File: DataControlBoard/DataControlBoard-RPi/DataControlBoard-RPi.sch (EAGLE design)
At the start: 6 parts, among them J1 USB3150-30-130-A, J2 USB3150-30-130-A, J3 USB3150-30-130-A, J4 USB3150-30-130-A, J5 USB3150-30-130-A, J6 USB3150-30-130-A

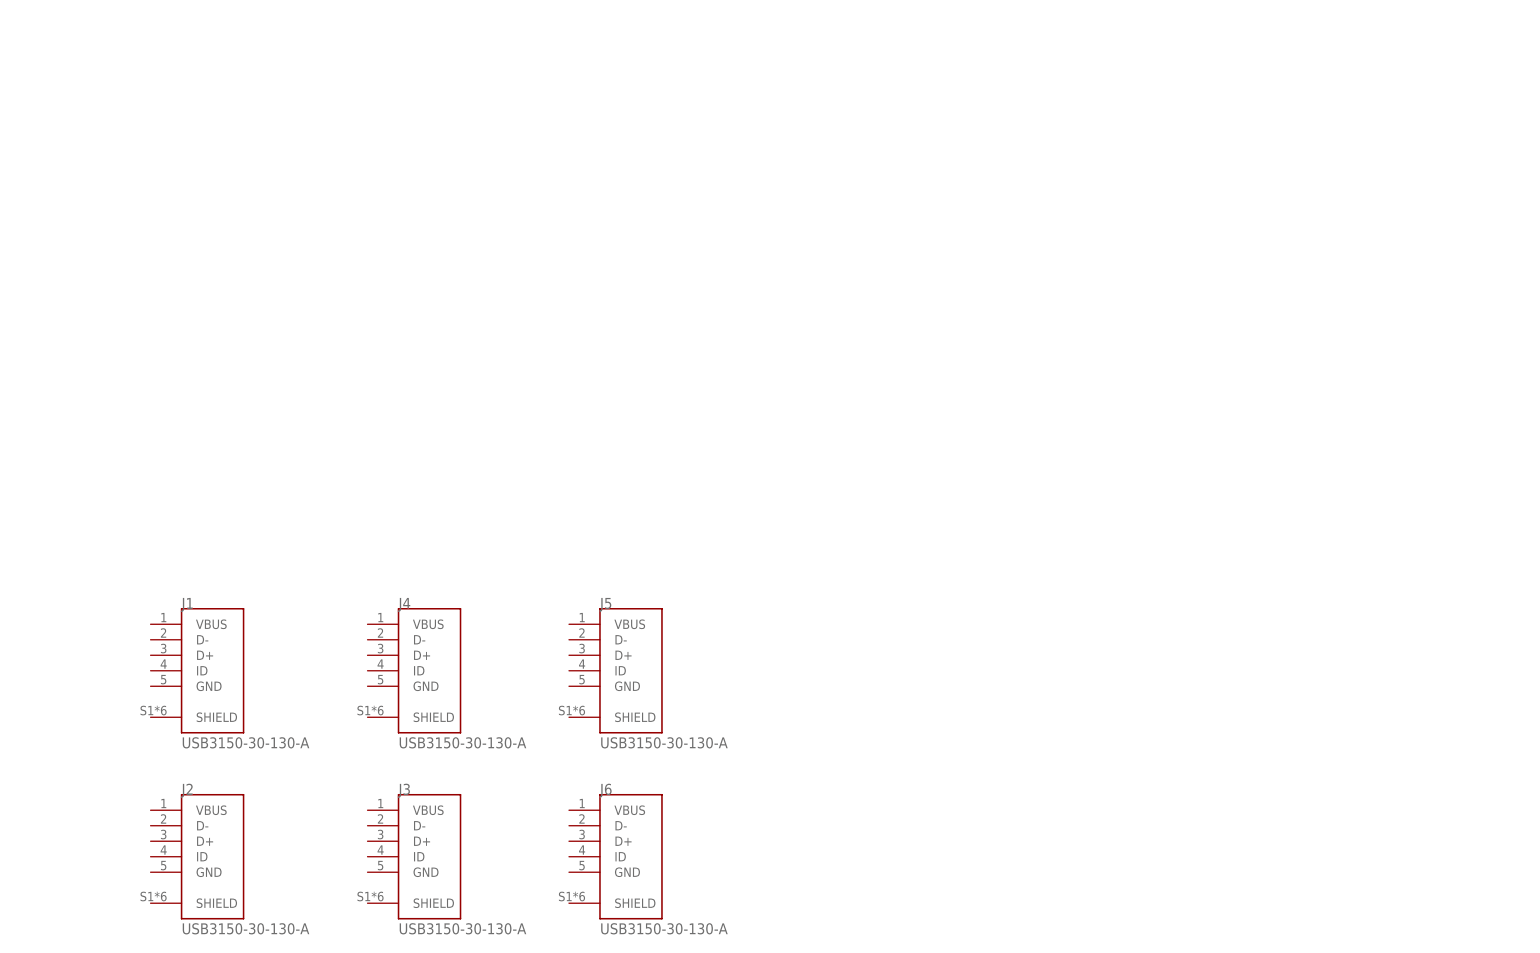
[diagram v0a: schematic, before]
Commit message: Added data control boards, further refined USB part
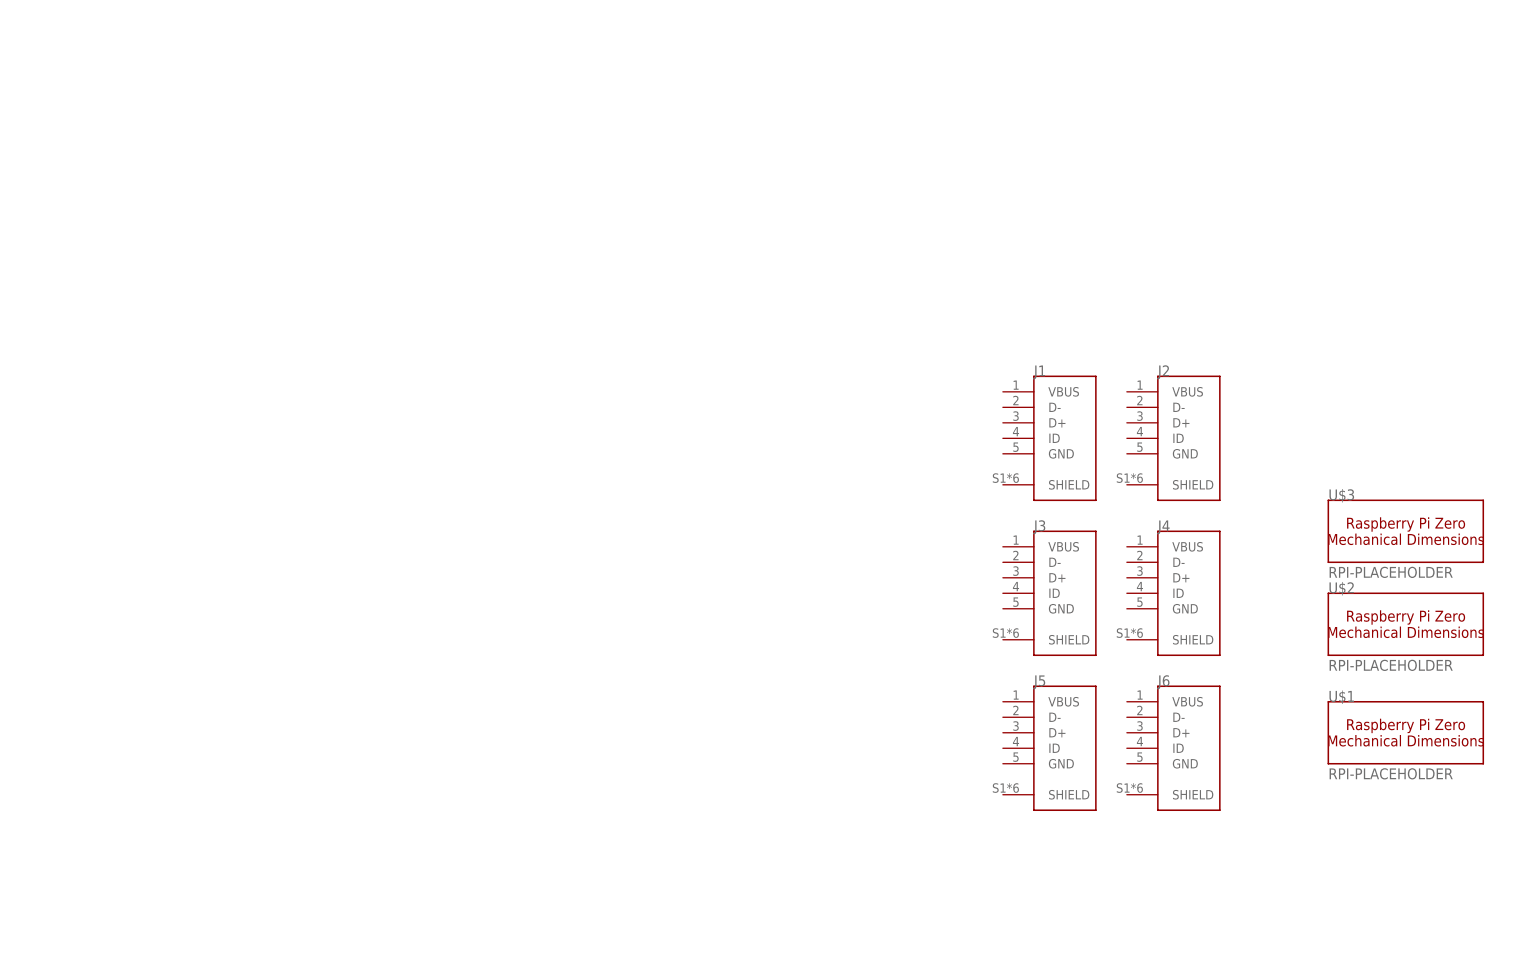
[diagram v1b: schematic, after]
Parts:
- added U$1, U$2, U$3: RPI-PLACEHOLDER, RPi-Parts:RPI-PLACEHOLDER
- J1, J2, J3, J4, J5, J6: value USB3150-30-130-A -> USB3150-30-130-AMANUFACTURABLE; device USB3150-30-130-A:USB3150-30-130-A -> RPi-Parts:USB3150-30-130-AMANUFACTURABLE
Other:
- moved on the sheet: J1, J2, J3, J4, J5, J6
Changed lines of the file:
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@@
 <layer number="97" name="Info" color="7" fill="1" visible="yes" active="yes"/>
 <layer number="98" name="Guide" color="6" fill="1" visible="yes" active="yes"/>
+<layer number="200" name="RPI-DIMS" color="39" fill="7" visible="yes" active="yes"/>
+<layer number="201" name="RPI-PORTS" color="22" fill="5" visible="yes" active="yes"/>
+<layer number="202" name="RPI-Mounting" color="23" fill="10" visible="yes" active="yes"/>
 </layers>
 <schematic xreflabel="%F%N/%S.%C%R" xrefpart="/%S.%C%R">
@@
 </classes>
 <parts>
-<part name="J1" library="USB3150-30-130-A" deviceset="USB3150-30-130-A" device=""/>
-<part name="J2" library="USB3150-30-130-A" deviceset="USB3150-30-130-A" device=""/>
-<part name="J3" library="USB3150-30-130-A" deviceset="USB3150-30-130-A" device=""/>
-<part name="J4" library="USB3150-30-130-A" deviceset="USB3150-30-130-A" device=""/>
-<part name="J5" library="USB3150-30-130-A" deviceset="USB3150-30-130-A" device=""/>
-<part name="J6" library="USB3150-30-130-A" deviceset="USB3150-30-130-A" device=""/>
 <part name="FRAME1" library="frames" library_urn="urn:adsk.eagle:library:229" deviceset="A4L-LOC" device=""/>
+<part name="U$1" library="RPi-Parts" deviceset="RPI-PLACEHOLDER" device=""/>
+<part name="U$2" library="RPi-Parts" deviceset="RPI-PLACEHOLDER" device=""/>
+<part name="U$3" library="RPi-Parts" deviceset="RPI-PLACEHOLDER" device=""/>
+<part name="J1" library="RPi-Parts" deviceset="USB3150-30-130-A" device="MANUFACTURABLE"/>
+<part name="J2" library="RPi-Parts" deviceset="USB3150-30-130-A" device="MANUFACTURABLE"/>
+<part name="J3" library="RPi-Parts" deviceset="USB3150-30-130-A" device="MANUFACTURABLE"/>
+<part name="J4" library="RPi-Parts" deviceset="USB3150-30-130-A" device="MANUFACTURABLE"/>
+<part name="J5" library="RPi-Parts" deviceset="USB3150-30-130-A" device="MANUFACTURABLE"/>
+<part name="J6" library="RPi-Parts" deviceset="USB3150-30-130-A" device="MANUFACTURABLE"/>
 </parts>
 <sheets>
@@
 </plain>
 <instances>
-<instance part="J1" gate="G$1" x="40.64" y="63.5" smashed="yes">
-<attribute name="NAME" x="35.56" y="73.66" size="1.778" layer="95"/>
-<attribute name="VALUE" x="35.56" y="50.8" size="1.778" layer="96"/>
-</instance>
-<instance part="J2" gate="G$1" x="40.64" y="33.02" smashed="yes">
-<attribute name="NAME" x="35.56" y="43.18" size="1.778" layer="95"/>
-<attribute name="VALUE" x="35.56" y="20.32" size="1.778" layer="96"/>
-</instance>
-<instance part="J3" gate="G$1" x="76.2" y="33.02" smashed="yes">
-<attribute name="NAME" x="71.12" y="43.18" size="1.778" layer="95"/>
-<attribute name="VALUE" x="71.12" y="20.32" size="1.778" layer="96"/>
-</instance>
-<instance part="J4" gate="G$1" x="76.2" y="63.5" smashed="yes">
-<attribute name="NAME" x="71.12" y="73.66" size="1.778" layer="95"/>
-<attribute name="VALUE" x="71.12" y="50.8" size="1.778" layer="96"/>
-</instance>
-<instance part="J5" gate="G$1" x="109.22" y="63.5" smashed="yes">
-<attribute name="NAME" x="104.14" y="73.66" size="1.778" layer="95"/>
-<attribute name="VALUE" x="104.14" y="50.8" size="1.778" layer="96"/>
-</instance>
-<instance part="J6" gate="G$1" x="109.22" y="33.02" smashed="yes">
-<attribute name="NAME" x="104.14" y="43.18" size="1.778" layer="95"/>
-<attribute name="VALUE" x="104.14" y="20.32" size="1.778" layer="96"/>
-</instance>
 <instance part="FRAME1" gate="G$1" x="0" y="0" smashed="yes">
 <attribute name="DRAWING_NAME" x="217.17" y="15.24" size="2.54" layer="94"/>
 <attribute name="LAST_DATE_TIME" x="217.17" y="10.16" size="2.286" layer="94"/>
 <attribute name="SHEET" x="230.505" y="5.08" size="2.54" layer="94"/>
+</instance>
+<instance part="U$1" gate="G$1" x="236.22" y="53.34" smashed="yes">
+<attribute name="NAME" x="223.52" y="58.42" size="1.778" layer="95"/>
+<attribute name="VALUE" x="223.52" y="45.72" size="1.778" layer="95"/>
+</instance>
+<instance part="U$2" gate="G$1" x="236.22" y="71.12" smashed="yes">
+<attribute name="NAME" x="223.52" y="76.2" size="1.778" layer="95"/>
+<attribute name="VALUE" x="223.52" y="63.5" size="1.778" layer="95"/>
+</instance>
+<instance part="U$3" gate="G$1" x="236.22" y="86.36" smashed="yes">
+<attribute name="NAME" x="223.52" y="91.44" size="1.778" layer="95"/>
+<attribute name="VALUE" x="223.52" y="78.74" size="1.778" layer="95"/>
+</instance>
+<instance part="J1" gate="G$1" x="180.34" y="101.6" smashed="yes">
+<attribute name="NAME" x="175.26" y="111.76" size="1.778" layer="95"/>
+</instance>
+<instance part="J2" gate="G$1" x="200.66" y="101.6" smashed="yes">
+<attribute name="NAME" x="195.58" y="111.76" size="1.778" layer="95"/>
+</instance>
+<instance part="J3" gate="G$1" x="180.34" y="76.2" smashed="yes">
+<attribute name="NAME" x="175.26" y="86.36" size="1.778" layer="95"/>
+</instance>
+<instance part="J4" gate="G$1" x="200.66" y="76.2" smashed="yes">
+<attribute name="NAME" x="195.58" y="86.36" size="1.778" layer="95"/>
+</instance>
+<instance part="J5" gate="G$1" x="180.34" y="50.8" smashed="yes">
+<attribute name="NAME" x="175.26" y="60.96" size="1.778" layer="95"/>
+</instance>
+<instance part="J6" gate="G$1" x="200.66" y="50.8" smashed="yes">
+<attribute name="NAME" x="195.58" y="60.96" size="1.778" layer="95"/>
 </instance>
 </instances>
@@
 </drawing>
 <compatibility>
+<note version="6.3" minversion="6.2.2" severity="warning">
+Since Version 6.2.2 text objects can contain more than one line,
+which will not be processed correctly with this version.
+</note>
 <note version="8.2" severity="warning">
 Since Version 8.2, EAGLE supports online libraries. The ids

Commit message: Mechanical design of RPi Holder board nearly done. Power treaces routed
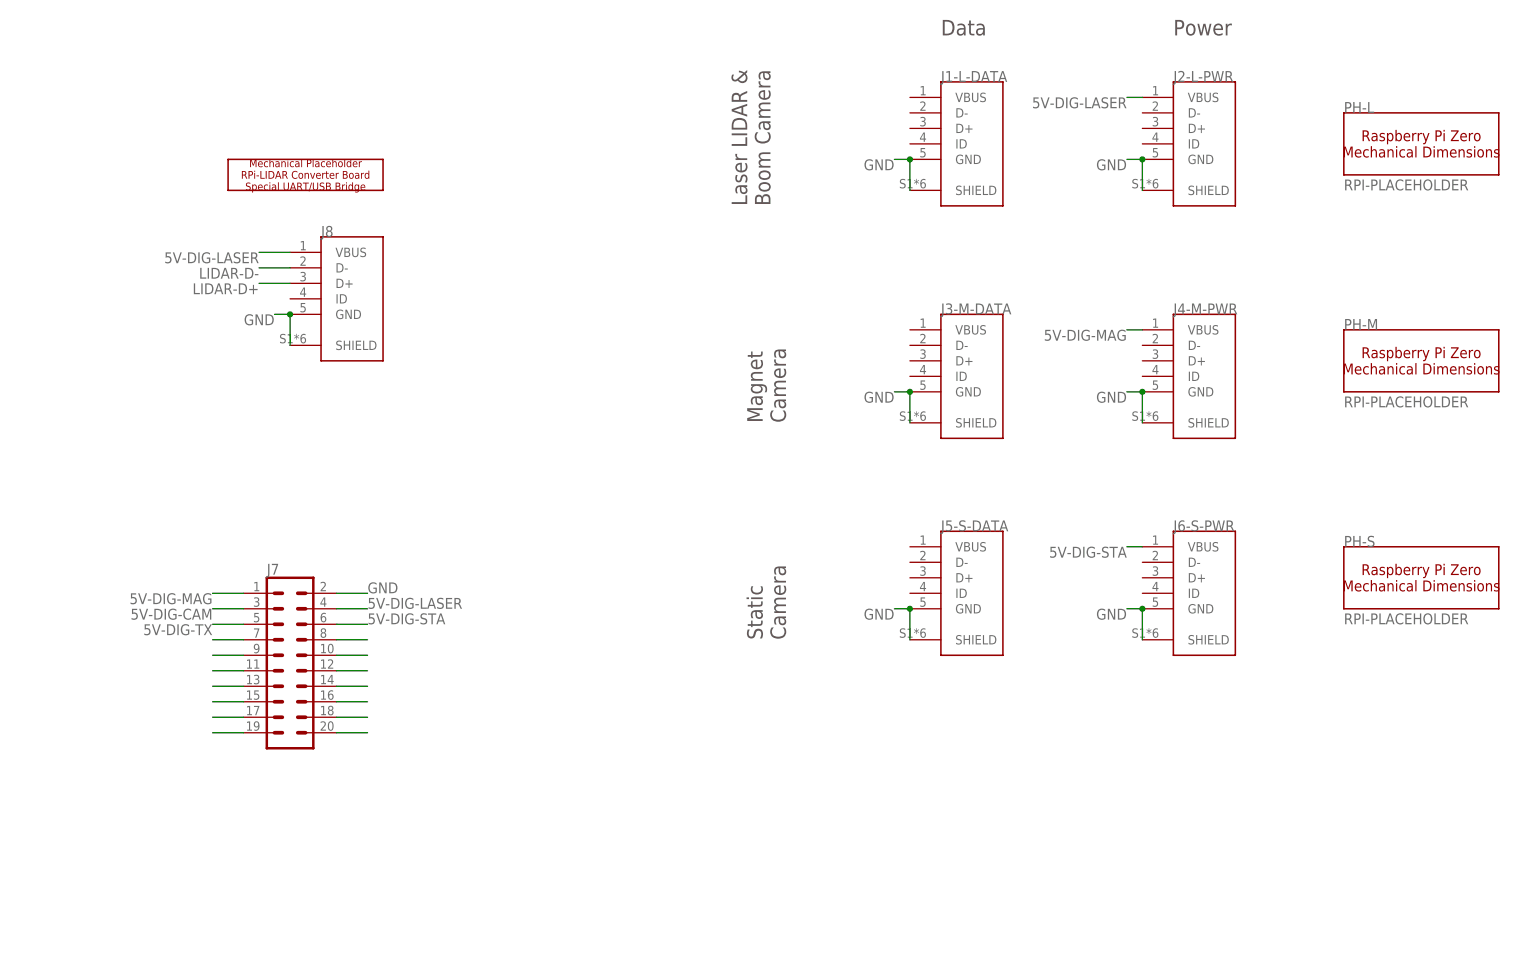
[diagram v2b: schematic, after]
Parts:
- removed J1, J2, J3, J4, J5, J6: USB3150-30-130-AMANUFACTURABLE, RPi-Parts:USB3150-30-130-AMANUFACTURABLE
- removed U$1, U$2, U$3: RPI-PLACEHOLDER, RPi-Parts:RPI-PLACEHOLDER
- added J1-L-DATA, J2-L-PWR, J3-M-DATA, J4-M-PWR, J5-S-DATA, J6-S-PWR, J8: USB3150-30-130-AMANUFACTURABLE, RPi-Parts:USB3150-30-130-AMANUFACTURABLE
- added J7: (no value), SparkFun-Connectors:CONN_10X2
- added PH-L, PH-M, PH-S: RPI-PLACEHOLDER, RPi-Parts:RPI-PLACEHOLDER
- added U$4: LIDAR-CONV-PLACEHOLDER, RPi-Parts:LIDAR-CONV-PLACEHOLDER
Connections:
- new net 5V-DIG-CAM: J7.3
- new net 5V-DIG-LASER: J2-L-PWR.VBUS, J7.4, J8.VBUS
- new net 5V-DIG-MAG: J4-M-PWR.VBUS, J7.1
- new net 5V-DIG-STA: J6-S-PWR.VBUS, J7.6
- new net 5V-DIG-TX: J7.5
- new net GND: J1-L-DATA.GND, J1-L-DATA.SHIELD, J2-L-PWR.GND, J2-L-PWR.SHIELD, J3-M-DATA.GND, J3-M-DATA.SHIELD, J4-M-PWR.GND, J4-M-PWR.SHIELD, J5-S-DATA.GND, J5-S-DATA.SHIELD, J6-S-PWR.GND, J6-S-PWR.SHIELD, J7.2, J8.GND, J8.SHIELD
- new net LIDAR-D+: J8.D+
- new net LIDAR-D-: J8.D-
- new net N$14: J7.7
- new net N$15: J7.9
- new net N$16: J7.11
- new net N$17: J7.13
- new net N$18: J7.15
- new net N$19: J7.17
- new net N$20: J7.19
- new net N$3: J7.20
- new net N$4: J7.18
- new net N$5: J7.16
- new net N$6: J7.14
- new net N$7: J7.12
- new net N$8: J7.10
- new net N$9: J7.8
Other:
- note added: "Data"
- note added: "Laser LIDAR & Boom Camera"
- note added: "Magnet Camera"
- note added: "Power"
- note added: "Static Camera"

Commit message: Added USB to all RPi boards. Rearranged mechanical design slightly
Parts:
- added J1, J2: USB3150-30-130-AMANUFACTURABLE, RPi-Parts:USB3150-30-130-AMANUFACTURABLE
- added J3: (no value), SparkFun-Connectors:CONN_03X22X3_SILK_MALE_PTH
- added TP1, TP2, TP3: TPPAD1-17, testpad:TPPAD1-17
- J7: value (none) -> FEMALE 2x3; device SparkFun-Connectors:CONN_10X2 -> SparkFun-Connectors:CONN_03X2FEMALE
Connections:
- removed net N$14: J7.7
- removed net N$15: J7.9
- removed net N$16: J7.11
- removed net N$17: J7.13
- removed net N$18: J7.15
- removed net N$19: J7.17
- removed net N$20: J7.19
- removed net N$5: J7.16
- removed net N$6: J7.14
- removed net N$7: J7.12
- removed net N$8: J7.10
- removed net N$9: J7.8
- new net MAG-D+: J1.D+, J3-M-DATA.D+
- new net MAG-D-: J1.D-, J3-M-DATA.D-
- new net N$2: J3.2, TP1.TP
- new net STA-D+: J2.D+, J5-S-DATA.D+
- new net STA-D-: J2.D-, J5-S-DATA.D-
- new net USB-5V-LID: J1-L-DATA.VBUS, J8.VBUS
- new net USB-5V-MAG: J1.VBUS, J3-M-DATA.VBUS
- new net USB-5V-STA: J2.VBUS, J5-S-DATA.VBUS
- net 5V-DIG-LASER: no longer J8.VBUS
- net GND: now also J1.GND, J1.SHIELD, J2.GND, J2.SHIELD, J3.1, J3.3, J3.5
- net LIDAR-D+: now also J1-L-DATA.D+
- net LIDAR-D-: now also J1-L-DATA.D-
- net N$3: now also J3.4, TP2.TP; no longer J7.20
- net N$4: now also J3.6, TP3.TP; no longer J7.18
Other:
- note added: "Misc connection points"
- note added: "Useful for correcting screw-ups"
- moved on the sheet: J8
